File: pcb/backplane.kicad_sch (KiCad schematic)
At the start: 0 parts

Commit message: schematic structure, added qspi flash, pinout defs. mostly work on PS pinouts, defining comms. buses, still need to choose dram part, phys, camera/bus, power supply etc
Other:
- note added: "samtec backplane connector"
- title: (none) -> CUTIE-CITRUS

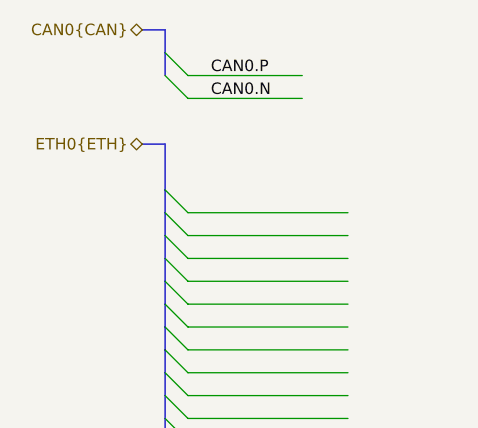
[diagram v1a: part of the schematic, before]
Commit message: edits to eth0 protocol names / bus aliases
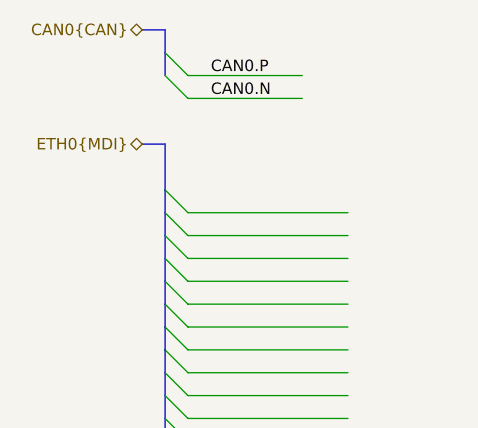
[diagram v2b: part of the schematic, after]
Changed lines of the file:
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@@
 		)
 	)
-	(hierarchical_label "ETH0{ETH}"
+	(hierarchical_label "ETH0{MDI}"
 		(shape bidirectional)
 		(at 116.84 101.6 180)
